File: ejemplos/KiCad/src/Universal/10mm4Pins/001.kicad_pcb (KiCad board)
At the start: 2 copper layers, 37.2 x 73.4 mm, 13 parts, among them J1 CONN_01X04

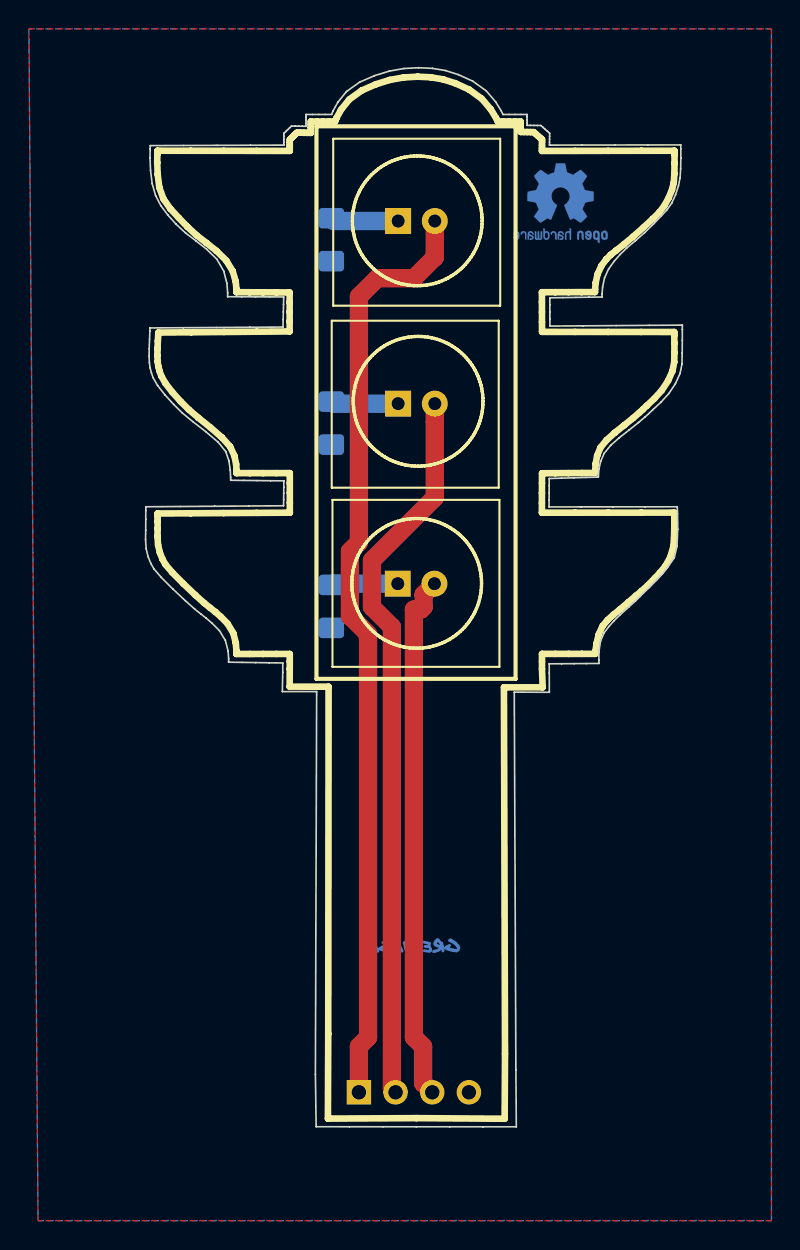
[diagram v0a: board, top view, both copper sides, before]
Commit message: Add Universal 4 Pin PCB
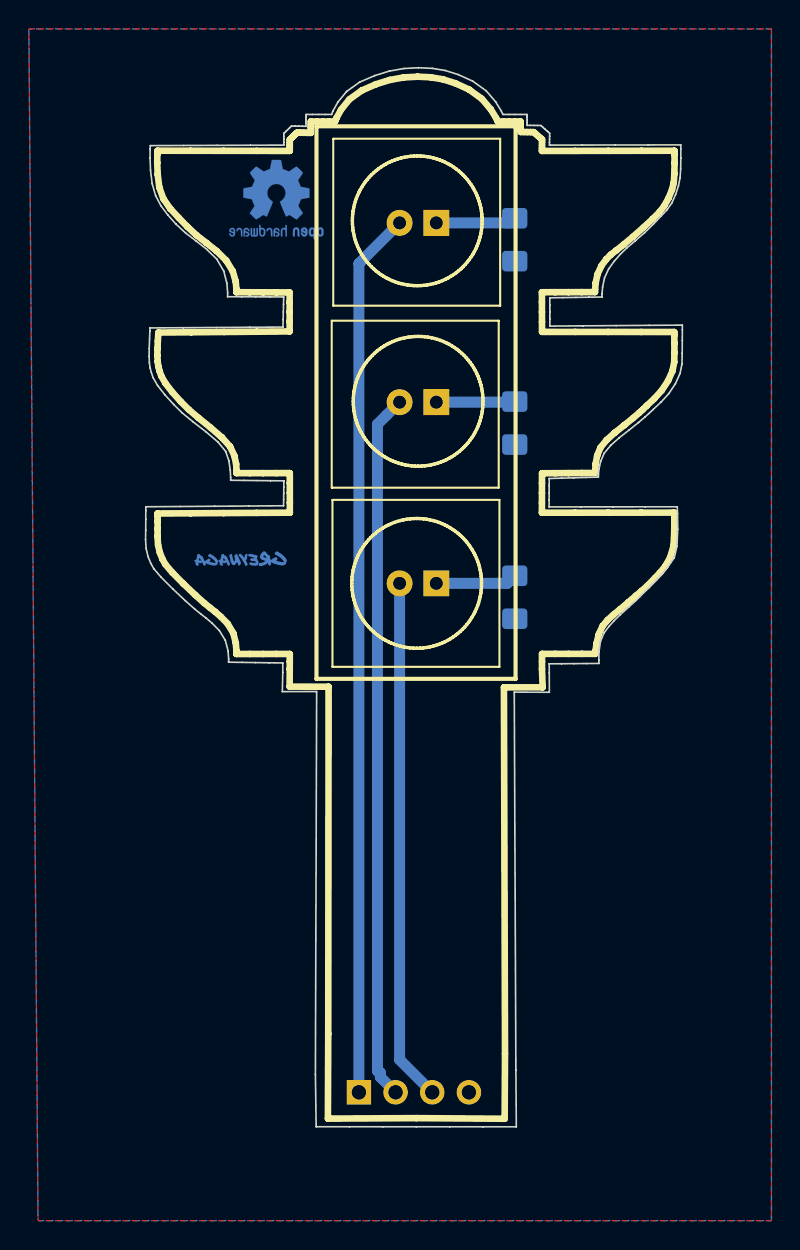
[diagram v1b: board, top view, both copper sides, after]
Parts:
- moved svg2mod 29.4 mm to (122.0, 106.6)
- moved svg2mod 29.2 mm to (121.8, 104.9)
- moved REF** 19.7 mm to (124.5, 81.7) (x2)
- moved R3 12.7 mm to (141.0, 109.2)
- moved R1 12.7 mm to (141.0, 84.5)
- moved R2 12.7 mm to (141.0, 97.2)
- moved D3 2.67 mm to (135.5, 108.3), turned to 180 degrees
- moved D1 2.64 mm to (135.5, 83.3), turned to 180 degrees
- moved D2 2.64 mm to (135.5, 95.7), turned to 180 degrees
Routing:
- net Net-(D1-Pad2): track 65.1 -> 61.4 mm
- net Net-(D2-Pad2): track 50.2 -> 49.0 mm
- net Net-(D3-Pad1): track 4.63 -> 5.65 mm
- net Net-(D1-Pad1): track 4.70 -> 5.57 mm
- net Net-(D2-Pad1): track 4.68 -> 5.45 mm
